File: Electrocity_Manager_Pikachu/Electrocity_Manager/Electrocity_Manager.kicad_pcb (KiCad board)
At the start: 2 copper layers, 100 x 77 mm, 190 parts, among them IC1 POW_ON, IC2 MAIN_SHUTDOWN, IC3 RELAY_STATE, IC4 ADC_RST, J1 SERIAL, P1 SWD, P10 EMERGENCY, P11 EMERGENCY, P12 FRAME_GRAND, P13 BATT_IN, P14 POWER_OUT, P15 FUN_OUT, P16 BATT_IN, P17 POWER_OUT, P18 FUN_OUT, P2 CAN, P3 CAN, P4 EMERGENCY_SIGNAL, P5 EMERGENCY_SIGNAL, P6 12V_OUT, P7 12V_OUT, P9 MAIN_SW, Q1 FET_N, Q2 NPN, Q3 NPN, Q7 FET_N, SW1 RST, SW2 SW0, SW3 SW1, U1 MAX3051, U10 NJM7812, U11 ACS781, U12 V23134J1052D642, U13 ACS70331, U14 ACS781, U15 BD33FA1, U16 LOGO, U17 LOGO, U18 LOGO, U19 MCP2221A, U2 STM32F405RG, U20 OSRB38C9AA, U21 OSRB38C9AA, U22 HSIN_946, U23 LOGO, U24 LOGO, U25 LOGO, U26 LOGO, U3 FULL COLOR, U4 AQM0802_BL, U5 AP3211, U6 SI8900, U7 AZ1086H, U8 V23134J1052D642, U9 RPA60-12FW/N, X1 8MHz

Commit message: ピカチュウたちの配線を変えた。
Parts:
- added U27: LOGO, Mizz_lib:kitLogo_Mask_5.0x5.0, B.Cu at (84.8, 129.0)
- added U28: LOGO, Mizz_lib:RedBull_Logo_Silk_16x16, F.Cu at (87.2, 169.0)
- C30, C31: footprint Mizz_lib:C_0603 -> Capacitors_SMD:C_0805
- moved U23 38.1 mm to (75.8, 120.5), turned to 180 degrees
- moved R47 3.00 mm to (121.0, 151.0)
- moved R44 2.85 mm to (113.8, 125.5)
- moved R40 1.35 mm to (112.2, 127.5)
- moved U24 0.56 mm to (93.5, 163.8)
- moved C31 0.25 mm to (87.0, 155.8)
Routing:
- net Net-(R47-Pad2): track 13.8 -> 17.2 mm
- net Net-(R40-Pad2): track 43.6 -> 46.1 mm
- net /ADC12_IN2: track 21.3 -> 18.9 mm
- net Net-(R44-Pad2): track 18.3 -> 20.6 mm
- net /ADC12_IN9: track 20.7 -> 19.6 mm
- net /ADC12_IN1: track 19.7 -> 18.6 mm
- net GNDPWR: vias 341 -> 302
- net GND: vias 111 -> 100
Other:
- board text added: "Pocket Monster -Pikachu-"
- board text removed: "Pocket Monster "Pikachu""

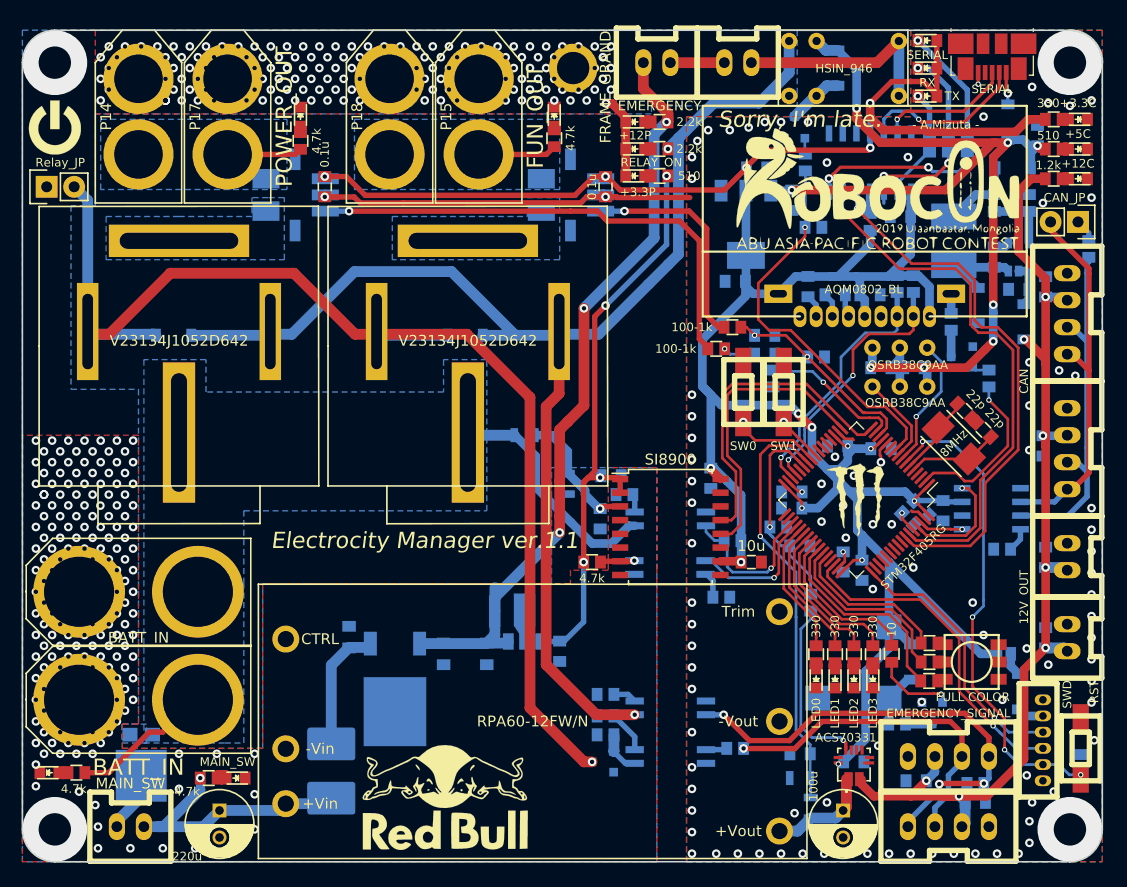
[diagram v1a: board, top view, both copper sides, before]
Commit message: 回路図,基板図を作成した.
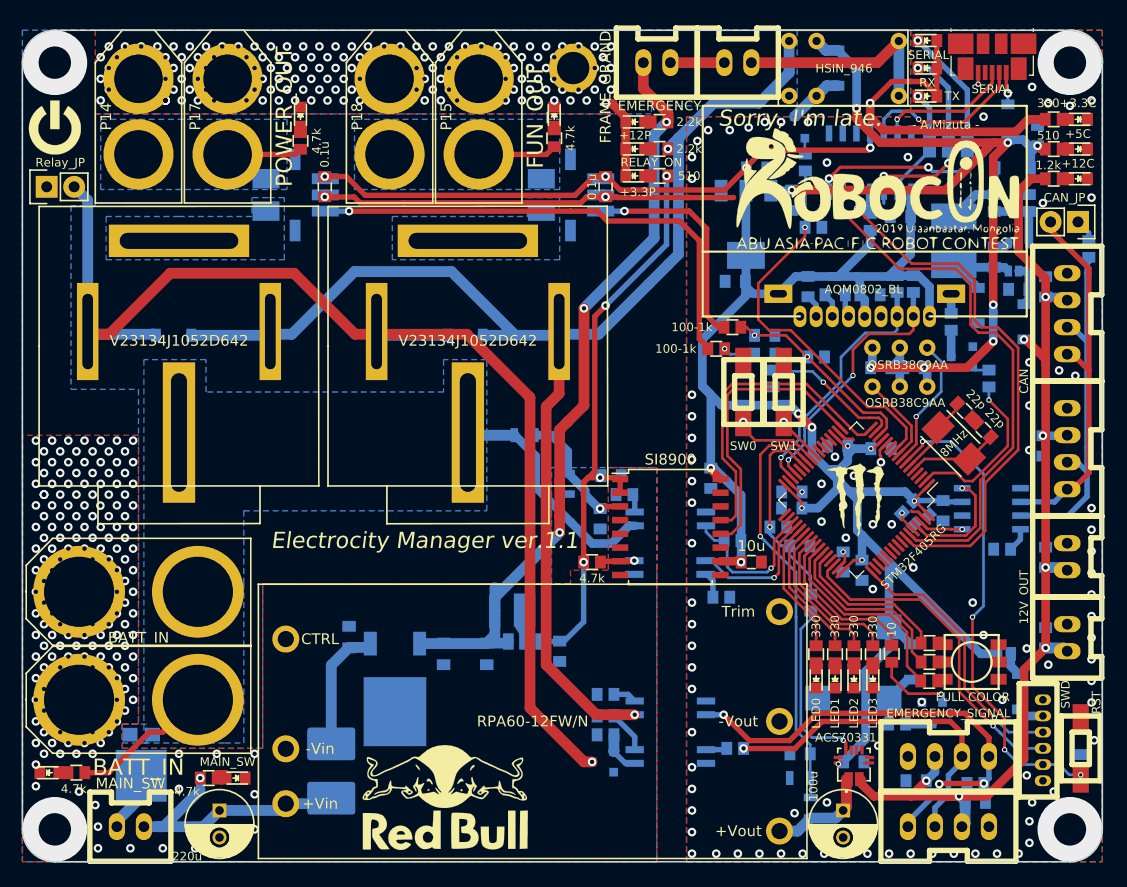
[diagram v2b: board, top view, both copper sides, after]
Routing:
- net GND: track 46.1 -> 50.4 mm
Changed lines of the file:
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@@
     (thickness 1.6)
     (drawings 37)
-    (tracks 1428)
+    (tracks 1430)
     (zones 0)
     (modules 192)
@@
   )
   (setup
-    (last_trace_width 0.25)
+    (last_trace_width 0.5)
     (user_trace_width 0.3)
     (user_trace_width 0.5)
@@
       (drillshape 0)
       (scaleselection 1)
-      (outputdirectory "C:/Users/Mizuta/Desktop/RC19_Circuit/Electrocity_Manager_Pikachu/加工データ/"))
+      (outputdirectory "C:/Users/Mizuta/Desktop/RC19_Circuit/Electrocity_Manager_Pikachu/Electrocity_Manager/"))
   )
   (net 0 "")
@@
       (effects (font (size 1 1) (thickness 0.15)))
     )
-    (fp_text value RST (at -5.25 -1.25 270) (layer F.SilkS)
+    (fp_text value RST (at -4.25 -1.45 270) (layer F.SilkS)
       (effects (font (size 0.8 0.8) (thickness 0.15)))
     )
@@
       (effects (font (size 1 1) (thickness 0.15)))
     )
-    (fp_text value SWD (at -0.5 -2.25 270) (layer F.SilkS)
+    (fp_text value SWD (at -0.5 -2.1 270) (layer F.SilkS)
       (effects (font (size 0.8 0.8) (thickness 0.2)))
     )
@@
       (effects (font (size 1 1) (thickness 0.15)))
     )
-    (fp_text value SERIAL (at 0 1.35) (layer F.SilkS)
+    (fp_text value SERIAL (at 0.1 1.35) (layer F.SilkS)
       (effects (font (size 0.8 0.8) (thickness 0.2)))
     )
@@
     (effects (font (size 0.8 0.8) (thickness 0.2)))
   )
-  (gr_text "Sorry, I'm late." (at 120 106.25) (layer F.SilkS)
+  (gr_text "Sorry, I'm late." (at 120 106.15) (layer F.SilkS)
     (effects (font (size 1.5 1.5) (thickness 0.375) italic))
   )
@@
   (segment (start 102.990037 113.43) (end 103.050037 113.49) (width 0.5) (layer F.Cu) (net 1))
   (segment (start 102 113.43) (end 102.990037 113.43) (width 0.5) (layer F.Cu) (net 1))
-  (segment (start 103.050037 113.49) (end 109.8 113.49) (width 0.5) (layer F.Cu) (net 1))
   (via (at 102 113.43) (size 0.8) (drill 0.4) (layers F.Cu B.Cu) (net 1) (status C00000))
   (segment (start 102 113.43) (end 101.82 113.25) (width 1) (layer B.Cu) (net 1) (status C00000))
@@
   (via (at 110 145.5) (size 0.8) (drill 0.4) (layers F.Cu B.Cu) (net 1))
   (via (at 110 137.75) (size 0.8) (drill 0.4) (layers F.Cu B.Cu) (net 1))
+  (segment (start 109.55 113.49) (end 113.86 113.49) (width 0.5) (layer F.Cu) (net 1))
+  (segment (start 109.55 113.49) (end 109.8 113.49) (width 0.5) (layer F.Cu) (net 1))
+  (segment (start 103.050037 113.49) (end 109.55 113.49) (width 0.5) (layer F.Cu) (net 1))
   (segment (start 131.525305 137.699569) (end 135.699569 137.699569) (width 0.25) (layer F.Cu) (net 2))
   (segment (start 130.517946 138.706928) (end 131.525305 137.699569) (width 0.25) (layer F.Cu) (net 2))

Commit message: ピカチュウ.
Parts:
- D10: footprint TO_SOT_Packages_SMD:TO-277A -> Package_TO_SOT_SMD:TO-277B
- moved D10 0.56 mm to (59.2, 166.5), turned to 180 degrees
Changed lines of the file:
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@@
   )
   (setup
-    (last_trace_width 0.5)
+    (last_trace_width 0.3)
     (user_trace_width 0.3)
     (user_trace_width 0.5)
@@
     )
   )
-  (module TO_SOT_Packages_SMD:TO-277A (layer B.Cu)
-    (at 59 166)
-    (descr "Thermal enhanced ultra thin SMD package; 3 leads; body: 5.8 x 4.3 x 0.78 mm")
-    (tags "TO-277A SOT-1289")
-    (fp_text reference D10 (at 0 4.318) (layer B.SilkS) hide
-      (effects (font (size 1 1) (thickness 0.15)) (justify mirror))
-    )
-    (fp_text value SBR_DIODE (at 3.25 1.25 90) (layer B.SilkS)
-      (effects (font (size 0.8 0.8) (thickness 0.15)) (justify mirror))
-    )
-    (fp_line (start 2.375 -1.75) (end 2.375 -3.325) (layer B.SilkS) (width 0.15))
-    (fp_line (start 2 -3.325) (end 2.375 -3.325) (layer B.SilkS) (width 0.15))
-    (fp_line (start -2.375 -1.75) (end -2.375 -3.325) (layer B.SilkS) (width 0.15))
-    (fp_line (start -2.375 -3.325) (end -2 -3.325) (layer B.SilkS) (width 0.15))
-    (pad 1 smd rect (at 1.04 -2.765) (size 1.4 1.27) (layers B.Cu B.Paste B.Mask)
-      (net 33 +BATT))
-    (pad 3 smd rect (at 0 1.04) (size 4.72 4.8) (layers B.Cu B.Paste B.Mask)
-      (net 34 "Net-(D10-Pad3)"))
-    (pad 2 smd rect (at -1.04 -2.765) (size 1.4 1.27) (layers B.Cu B.Paste B.Mask)
-      (net 33 +BATT))
-    (model TO_SOT_Packages_SMD.3dshapes/TO-277A.wrl
-      (at (xyz 0 0 0))
-      (scale (xyz 1 1 1))
-      (rotate (xyz 0 0 0))
-    )
-  )
   (module Mizz_lib:LED_0603 (layer F.Cu)
     (at 50.5 166.75)
@@
       (at (xyz 0 0 0))
       (scale (xyz 1 1 1))
+      (rotate (xyz 0 0 0))
+    )
+  )
+  (module Package_TO_SOT_SMD:TO-277B (layer B.Cu)
+    (at 59.25 166.5 180)
+    (descr "TO-227B https://media.digikey.com/pdf/Data%20Sheets/Littelfuse%20PDFs/DST2050S.pdf")
+    (tags TO-277B)
+    (attr smd)
+    (fp_text reference D10 (at 0 4.6) (layer B.SilkS) hide
+      (effects (font (size 1 1) (thickness 0.15)) (justify mirror))
+    )
+    (fp_text value SBR_DIODE (at 2.75 0 90) (layer B.SilkS)
+      (effects (font (size 0.8 0.8) (thickness 0.2)) (justify mirror))
+    )
+    (fp_text user %R (at 0 0 180) (layer B.Fab)
+      (effects (font (size 0.9 0.9) (thickness 0.15)) (justify mirror))
+    )
+    (fp_line (start 2.11 2.81) (end 1.7 2.81) (layer B.SilkS) (width 0.12))
+    (fp_line (start -1.7 2.81) (end -2.11 2.81) (layer B.SilkS) (width 0.12))
+    (fp_line (start -2.11 2.81) (end -2.11 -2.81) (layer B.SilkS) (width 0.12))
+    (fp_line (start 2.11 -2.81) (end 2.11 2.81) (layer B.SilkS) (width 0.12))
+    (fp_line (start 1.99 -2.69) (end 1.99 2.69) (layer B.Fab) (width 0.1))
+    (fp_line (start 1.99 2.69) (end -1 2.69) (layer B.Fab) (width 0.1))
+    (fp_line (start -1.99 1.69) (end -1.99 -2.69) (layer B.Fab) (width 0.1))
+    (fp_line (start -1.99 -2.69) (end 1.99 -2.69) (layer B.Fab) (width 0.1))
+    (fp_line (start 1.85 -3.9) (end -1.85 -3.9) (layer B.CrtYd) (width 0.05))
+    (fp_line (start 2.24 -2.94) (end 2.24 2.94) (layer B.CrtYd) (width 0.05))
+    (fp_line (start -2.24 2.94) (end -2.24 -2.94) (layer B.CrtYd) (width 0.05))
+    (fp_line (start -1.7 3.9) (end 1.7 3.9) (layer B.CrtYd) (width 0.05))
+    (fp_line (start -1.7 2.81) (end -1.7 3.6) (layer B.SilkS) (width 0.12))
+    (fp_line (start 2.11 -2.81) (end 1.85 -2.81) (layer B.SilkS) (width 0.12))
+    (fp_line (start -1.85 -2.81) (end -2.11 -2.81) (layer B.SilkS) (width 0.12))
+    (fp_line (start -1.99 1.69) (end -0.99 2.69) (layer B.Fab) (width 0.1))
+    (fp_line (start -2.24 2.94) (end -1.7 2.94) (layer B.CrtYd) (width 0.05))
+    (fp_line (start -1.7 2.94) (end -1.7 3.9) (layer B.CrtYd) (width 0.05))
+    (fp_line (start 1.7 2.94) (end 1.7 3.9) (layer B.CrtYd) (width 0.05))
+    (fp_line (start 1.7 2.94) (end 2.24 2.94) (layer B.CrtYd) (width 0.05))
+    (fp_line (start -2.24 -2.94) (end -1.85 -2.94) (layer B.CrtYd) (width 0.05))
+    (fp_line (start -1.85 -3.9) (end -1.85 -2.94) (layer B.CrtYd) (width 0.05))
+    (fp_line (start 1.85 -3.9) (end 1.85 -2.94) (layer B.CrtYd) (width 0.05))
+    (fp_line (start 1.85 -2.94) (end 2.24 -2.94) (layer B.CrtYd) (width 0.05))
+    (pad 1 smd rect (at -0.97 3.15 180) (size 0.95 1) (layers B.Cu B.Paste B.Mask)
+      (net 33 +BATT))
+    (pad 3 smd rect (at 0 -1.2 180) (size 3.2 4.9) (layers B.Cu B.Mask)
+      (net 34 "Net-(D10-Pad3)"))
+    (pad 2 smd rect (at 0.97 3.15 180) (size 0.95 1) (layers B.Cu B.Paste B.Mask)
+      (net 33 +BATT))
+    (pad "" smd rect (at -0.9 0.6 180) (size 1.3 1.2) (layers B.Paste))
+    (pad "" smd rect (at -0.9 -1.2 180) (size 1.3 1.2) (layers B.Paste))
+    (pad "" smd rect (at 0.9 0.6 180) (size 1.3 1.2) (layers B.Paste))
+    (pad "" smd rect (at 0.9 -1.2 180) (size 1.3 1.2) (layers B.Paste))
+    (pad "" smd rect (at -0.9 -3 180) (size 1.3 1.2) (layers B.Paste))
+    (pad "" smd rect (at 0.9 -3 180) (size 1.3 1.2) (layers B.Paste))
+    (model ${KISYS3DMOD}/Package_TO_SOT_SMD.3dshapes/TO-277B.wrl
+      (at (xyz 0 0 0))
+      (scale (xyz 1 1 1))
